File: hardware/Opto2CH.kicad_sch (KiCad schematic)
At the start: 5 parts

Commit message: 3d models update, more work on pcb
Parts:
- renumbered O2 to O3, R40 to R14, R44 to R16, R45 to R75, R67 to R76
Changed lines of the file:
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@@
   (symbol (lib_id "power:+3.3V") (at 163.195 88.265 0)
     (in_bom yes) (on_board yes)
-    (property "Reference" "#PWR0161" (id 0) (at 163.195 92.075 0)
+    (property "Reference" "#PWR0165" (id 0) (at 163.195 92.075 0)
       (effects (font (size 1.27 1.27)) hide)
     )
@@
   (symbol (lib_id "Device:R") (at 131.445 98.425 270)
     (in_bom yes) (on_board yes)
-    (property "Reference" "R40" (id 0) (at 131.445 93.1672 90))
+    (property "Reference" "R14" (id 0) (at 131.445 93.1672 90))
     (property "Value" "3.3k" (id 1) (at 131.445 95.4786 90))
     (property "Footprint" "Resistor_SMD:R_0603_1608Metric" (id 2) (at 131.445 96.647 90)
@@
   (symbol (lib_id "Device:R") (at 163.195 93.345 180)
     (in_bom yes) (on_board yes)
-    (property "Reference" "R67" (id 0) (at 164.973 92.1766 0)
+    (property "Reference" "R76" (id 0) (at 164.973 92.1766 0)
       (effects (font (size 1.27 1.27)) (justify right))
     )
@@
   (symbol (lib_id "Opto 2 ch:FOD8802DR2_IMG") (at 146.685 93.345 0)
     (in_bom yes) (on_board yes)
-    (property "Reference" "O2" (id 0) (at 144.78 92.71 0))
+    (property "Reference" "O3" (id 0) (at 144.78 92.71 0))
     (property "Value" "FOD8802DR2_IMG" (id 1) (at 144.145 94.615 0))
     (property "Footprint" "Opto 2 ch:SOIC127P600X175-8N" (id 2) (at 146.685 93.345 0)
@@
   (symbol (lib_id "power:GND") (at 154.305 114.935 0)
     (in_bom yes) (on_board yes)
-    (property "Reference" "#PWR0158" (id 0) (at 154.305 121.285 0)
+    (property "Reference" "#PWR0162" (id 0) (at 154.305 121.285 0)
       (effects (font (size 1.27 1.27)) hide)
     )
@@
   (symbol (lib_id "power:+3.3V") (at 155.575 88.265 0)
     (in_bom yes) (on_board yes)
-    (property "Reference" "#PWR0160" (id 0) (at 155.575 92.075 0)
+    (property "Reference" "#PWR0164" (id 0) (at 155.575 92.075 0)
       (effects (font (size 1.27 1.27)) hide)
     )
@@
   (symbol (lib_id "Device:R") (at 155.575 93.345 180)
     (in_bom yes) (on_board yes)
-    (property "Reference" "R45" (id 0) (at 157.353 92.1766 0)
+    (property "Reference" "R75" (id 0) (at 157.353 92.1766 0)
       (effects (font (size 1.27 1.27)) (justify right))
     )
@@
   (symbol (lib_id "Device:R") (at 131.445 107.315 270)
     (in_bom yes) (on_board yes)
-    (property "Reference" "R44" (id 0) (at 131.445 102.0572 90))
+    (property "Reference" "R16" (id 0) (at 131.445 102.0572 90))
     (property "Value" "3.3k" (id 1) (at 131.445 104.3686 90))
     (property "Footprint" "Resistor_SMD:R_0603_1608Metric" (id 2) (at 131.445 105.537 90)
@@
   (symbol (lib_id "power:GND") (at 136.525 114.935 0)
     (in_bom yes) (on_board yes)
-    (property "Reference" "#PWR0159" (id 0) (at 136.525 121.285 0)
+    (property "Reference" "#PWR0163" (id 0) (at 136.525 121.285 0)
       (effects (font (size 1.27 1.27)) hide)
     )

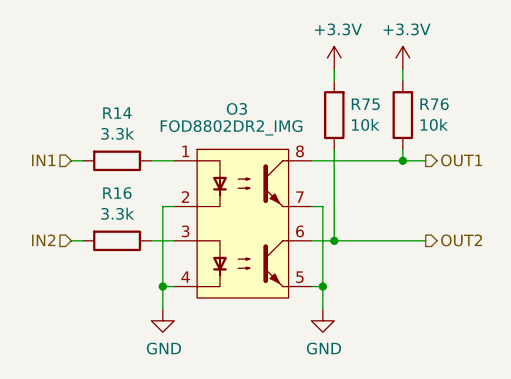
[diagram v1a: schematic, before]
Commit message: Schematic readability update
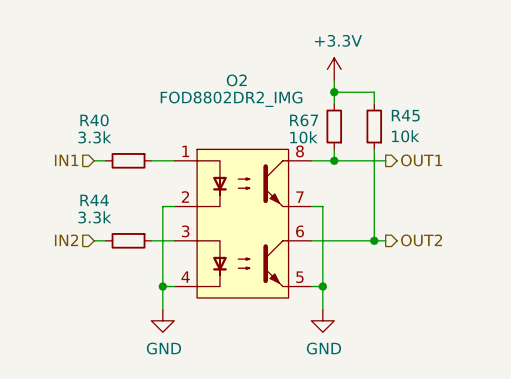
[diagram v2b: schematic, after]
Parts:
- R40: renamed from R14; symbol Device:R -> Device:R_Small
- R44: renamed from R16; symbol Device:R -> Device:R_Small
- R45: renamed from R75; symbol Device:R -> Device:R_Small
- R67: renamed from R76; symbol Device:R -> Device:R_Small
- renumbered O3 to O2
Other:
- moved on the sheet: R40, R44, R45, R67

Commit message: finished pcb layout, started routing, changed 2 layered board to 4 layered'
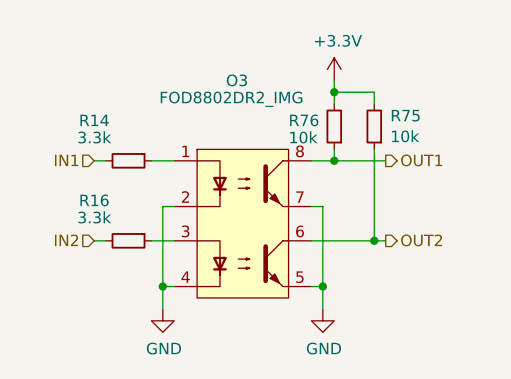
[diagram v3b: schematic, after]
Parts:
- renumbered O2 to O3, R40 to R14, R44 to R16, R45 to R75, R67 to R76
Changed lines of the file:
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@@
   (symbol (lib_id "Device:R_Small") (at 132.715 98.425 270)
     (in_bom yes) (on_board yes)
-    (property "Reference" "R40" (id 0) (at 128.905 93.98 90))
+    (property "Reference" "R14" (id 0) (at 128.905 93.98 90))
     (property "Value" "3.3k" (id 1) (at 128.905 95.885 90))
     (property "Footprint" "Resistor_SMD:R_0603_1608Metric" (id 2) (at 132.715 98.425 0)
@@
   (symbol (lib_id "power:GND") (at 154.305 114.935 0)
     (in_bom yes) (on_board yes)
-    (property "Reference" "#PWR?" (id 0) (at 154.305 121.285 0)
+    (property "Reference" "#PWR0177" (id 0) (at 154.305 121.285 0)
       (effects (font (size 1.27 1.27)) hide)
     )
@@
   (symbol (lib_id "Device:R_Small") (at 155.575 94.615 180)
     (in_bom yes) (on_board yes)
-    (property "Reference" "R67" (id 0) (at 150.495 93.98 0)
+    (property "Reference" "R76" (id 0) (at 150.495 93.98 0)
       (effects (font (size 1.27 1.27)) (justify right))
     )
@@
   (symbol (lib_id "Opto 2 ch:FOD8802DR2_IMG") (at 146.685 93.345 0)
     (in_bom yes) (on_board yes)
-    (property "Reference" "O2" (id 0) (at 144.78 89.535 0))
+    (property "Reference" "O3" (id 0) (at 144.78 89.535 0))
     (property "Value" "FOD8802DR2_IMG" (id 1) (at 144.145 91.44 0))
     (property "Footprint" "Opto 2 ch:SOIC127P600X175-8N" (id 2) (at 146.685 93.345 0)
@@
   (symbol (lib_id "power:GND") (at 136.525 114.935 0)
     (in_bom yes) (on_board yes)
-    (property "Reference" "#PWR?" (id 0) (at 136.525 121.285 0)
+    (property "Reference" "#PWR0178" (id 0) (at 136.525 121.285 0)
       (effects (font (size 1.27 1.27)) hide)
     )
@@
   (symbol (lib_id "Device:R_Small") (at 160.02 94.615 180)
     (in_bom yes) (on_board yes)
-    (property "Reference" "R45" (id 0) (at 161.798 93.4466 0)
+    (property "Reference" "R75" (id 0) (at 161.798 93.4466 0)
       (effects (font (size 1.27 1.27)) (justify right))
     )
@@
   (symbol (lib_id "Device:R_Small") (at 132.715 107.315 270)
     (in_bom yes) (on_board yes)
-    (property "Reference" "R44" (id 0) (at 128.905 102.87 90))
+    (property "Reference" "R16" (id 0) (at 128.905 102.87 90))
     (property "Value" "3.3k" (id 1) (at 128.905 104.775 90))
     (property "Footprint" "Resistor_SMD:R_0603_1608Metric" (id 2) (at 132.715 107.315 0)

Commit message: schematic override, just cuz
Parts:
- renumbered O3 to O2, R14 to R40, R16 to R44, R75 to R45, R76 to R67
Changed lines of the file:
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@@
   (symbol (lib_id "power:+3.3V") (at 155.575 89.535 0)
     (in_bom yes) (on_board yes)
-    (property "Reference" "#PWR0165" (id 0) (at 155.575 93.345 0)
+    (property "Reference" "#PWR0161" (id 0) (at 155.575 93.345 0)
       (effects (font (size 1.27 1.27)) hide)
     )
@@
   (symbol (lib_id "Device:R_Small") (at 132.715 98.425 270)
     (in_bom yes) (on_board yes)
-    (property "Reference" "R14" (id 0) (at 128.905 93.98 90))
+    (property "Reference" "R40" (id 0) (at 128.905 93.98 90))
     (property "Value" "3.3k" (id 1) (at 128.905 95.885 90))
     (property "Footprint" "Resistor_SMD:R_0603_1608Metric" (id 2) (at 132.715 98.425 0)
@@
   (symbol (lib_id "power:GND") (at 154.305 114.935 0)
     (in_bom yes) (on_board yes)
-    (property "Reference" "#PWR0159" (id 0) (at 154.305 121.285 0)
+    (property "Reference" "#PWR0177" (id 0) (at 154.305 121.285 0)
       (effects (font (size 1.27 1.27)) hide)
     )
@@
   (symbol (lib_id "Device:R_Small") (at 155.575 94.615 180)
     (in_bom yes) (on_board yes)
-    (property "Reference" "R76" (id 0) (at 150.495 93.98 0)
+    (property "Reference" "R67" (id 0) (at 150.495 93.98 0)
       (effects (font (size 1.27 1.27)) (justify right))
     )
@@
   (symbol (lib_id "Opto 2 ch:FOD8802DR2_IMG") (at 146.685 93.345 0)
     (in_bom yes) (on_board yes)
-    (property "Reference" "O3" (id 0) (at 144.78 89.535 0))
+    (property "Reference" "O2" (id 0) (at 144.78 89.535 0))
     (property "Value" "FOD8802DR2_IMG" (id 1) (at 144.145 91.44 0))
     (property "Footprint" "Opto 2 ch:SOIC127P600X175-8N" (id 2) (at 146.685 93.345 0)
@@
   (symbol (lib_id "power:GND") (at 136.525 114.935 0)
     (in_bom yes) (on_board yes)
-    (property "Reference" "#PWR0160" (id 0) (at 136.525 121.285 0)
+    (property "Reference" "#PWR0178" (id 0) (at 136.525 121.285 0)
       (effects (font (size 1.27 1.27)) hide)
     )
@@
   (symbol (lib_id "Device:R_Small") (at 160.02 94.615 180)
     (in_bom yes) (on_board yes)
-    (property "Reference" "R75" (id 0) (at 161.798 93.4466 0)
+    (property "Reference" "R45" (id 0) (at 161.798 93.4466 0)
       (effects (font (size 1.27 1.27)) (justify right))
     )
@@
   (symbol (lib_id "Device:R_Small") (at 132.715 107.315 270)
     (in_bom yes) (on_board yes)
-    (property "Reference" "R16" (id 0) (at 128.905 102.87 90))
+    (property "Reference" "R44" (id 0) (at 128.905 102.87 90))
     (property "Value" "3.3k" (id 1) (at 128.905 104.775 90))
     (property "Footprint" "Resistor_SMD:R_0603_1608Metric" (id 2) (at 132.715 107.315 0)

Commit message: hv elem positioning update'
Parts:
- renumbered O2 to O3, R40 to R14, R44 to R16, R45 to R75, R67 to R76
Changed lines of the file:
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@@
   (symbol (lib_id "power:+3.3V") (at 155.575 89.535 0)
     (in_bom yes) (on_board yes)
-    (property "Reference" "#PWR0161" (id 0) (at 155.575 93.345 0)
+    (property "Reference" "#PWR0165" (id 0) (at 155.575 93.345 0)
       (effects (font (size 1.27 1.27)) hide)
     )
@@
   (symbol (lib_id "Device:R_Small") (at 132.715 98.425 270)
     (in_bom yes) (on_board yes)
-    (property "Reference" "R40" (id 0) (at 128.905 93.98 90))
+    (property "Reference" "R14" (id 0) (at 128.905 93.98 90))
     (property "Value" "3.3k" (id 1) (at 128.905 95.885 90))
     (property "Footprint" "Resistor_SMD:R_0603_1608Metric" (id 2) (at 132.715 98.425 0)
@@
   (symbol (lib_id "power:GND") (at 154.305 114.935 0)
     (in_bom yes) (on_board yes)
-    (property "Reference" "#PWR0177" (id 0) (at 154.305 121.285 0)
+    (property "Reference" "#PWR0159" (id 0) (at 154.305 121.285 0)
       (effects (font (size 1.27 1.27)) hide)
     )
@@
   (symbol (lib_id "Device:R_Small") (at 155.575 94.615 180)
     (in_bom yes) (on_board yes)
-    (property "Reference" "R67" (id 0) (at 150.495 93.98 0)
+    (property "Reference" "R76" (id 0) (at 150.495 93.98 0)
       (effects (font (size 1.27 1.27)) (justify right))
     )
@@
   (symbol (lib_id "Opto 2 ch:FOD8802DR2_IMG") (at 146.685 93.345 0)
     (in_bom yes) (on_board yes)
-    (property "Reference" "O2" (id 0) (at 144.78 89.535 0))
+    (property "Reference" "O3" (id 0) (at 144.78 89.535 0))
     (property "Value" "FOD8802DR2_IMG" (id 1) (at 144.145 91.44 0))
     (property "Footprint" "Opto 2 ch:SOIC127P600X175-8N" (id 2) (at 146.685 93.345 0)
@@
   (symbol (lib_id "power:GND") (at 136.525 114.935 0)
     (in_bom yes) (on_board yes)
-    (property "Reference" "#PWR0178" (id 0) (at 136.525 121.285 0)
+    (property "Reference" "#PWR0160" (id 0) (at 136.525 121.285 0)
       (effects (font (size 1.27 1.27)) hide)
     )
@@
   (symbol (lib_id "Device:R_Small") (at 160.02 94.615 180)
     (in_bom yes) (on_board yes)
-    (property "Reference" "R45" (id 0) (at 161.798 93.4466 0)
+    (property "Reference" "R75" (id 0) (at 161.798 93.4466 0)
       (effects (font (size 1.27 1.27)) (justify right))
     )
@@
   (symbol (lib_id "Device:R_Small") (at 132.715 107.315 270)
     (in_bom yes) (on_board yes)
-    (property "Reference" "R44" (id 0) (at 128.905 102.87 90))
+    (property "Reference" "R16" (id 0) (at 128.905 102.87 90))
     (property "Value" "3.3k" (id 1) (at 128.905 104.775 90))
     (property "Footprint" "Resistor_SMD:R_0603_1608Metric" (id 2) (at 132.715 107.315 0)

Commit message: remake in progress
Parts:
- renumbered O3 to O2, R14 to R40, R16 to R44, R75 to R45, R76 to R67
